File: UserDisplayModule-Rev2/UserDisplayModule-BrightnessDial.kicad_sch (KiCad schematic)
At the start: 4 parts, among them U2 LM324

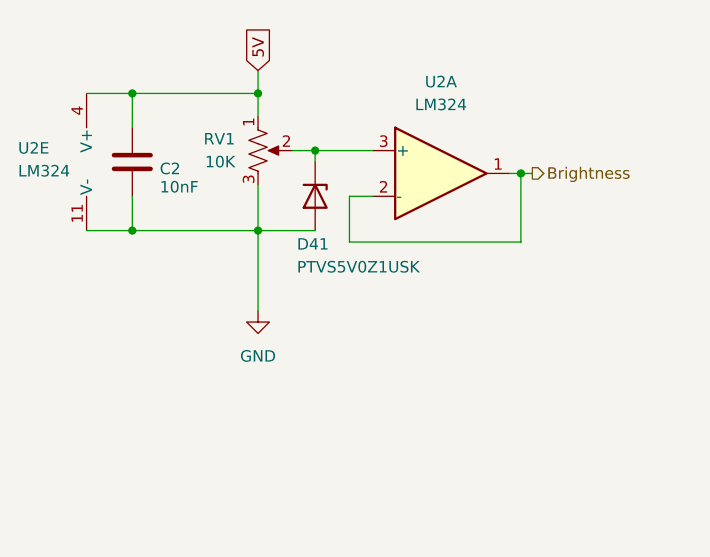
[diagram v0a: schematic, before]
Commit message: more changes: ldo bypass + grounding op amp
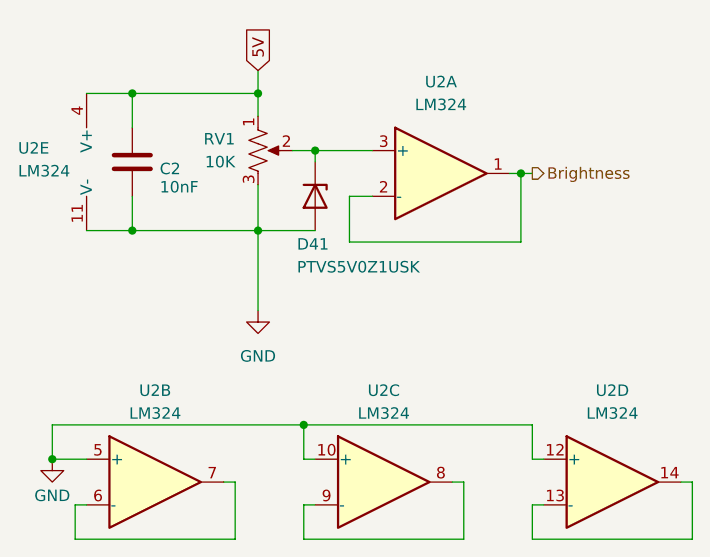
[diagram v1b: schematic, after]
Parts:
- added unit 3 of U2
- added unit 2 of U2
- added unit 4 of U2
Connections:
- net GND: now also U2.10 (+), U2.12 (+), U2.5 (+)
- new net: U2.8, U2.9 (-)
- new net: U2.6 (-), U2.7
- new net: U2.13 (-), U2.14
